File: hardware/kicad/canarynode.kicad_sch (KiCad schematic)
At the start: 26 parts, among them J1 Conn_01x02_Pin, SW1 SW_Push, U1 TPS62160DGK, U2 STM32G474RETx

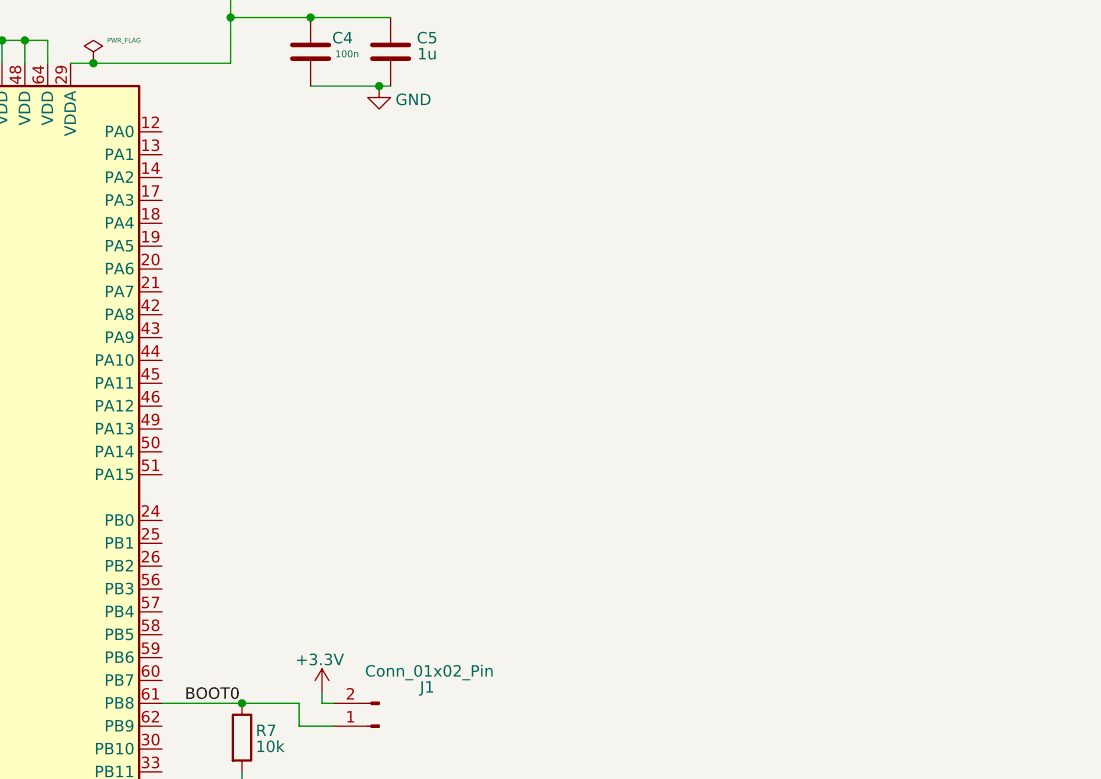
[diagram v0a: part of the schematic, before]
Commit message: schematic: add USB-C subcircuit (J2, U3, R8/R9, C14/C15)
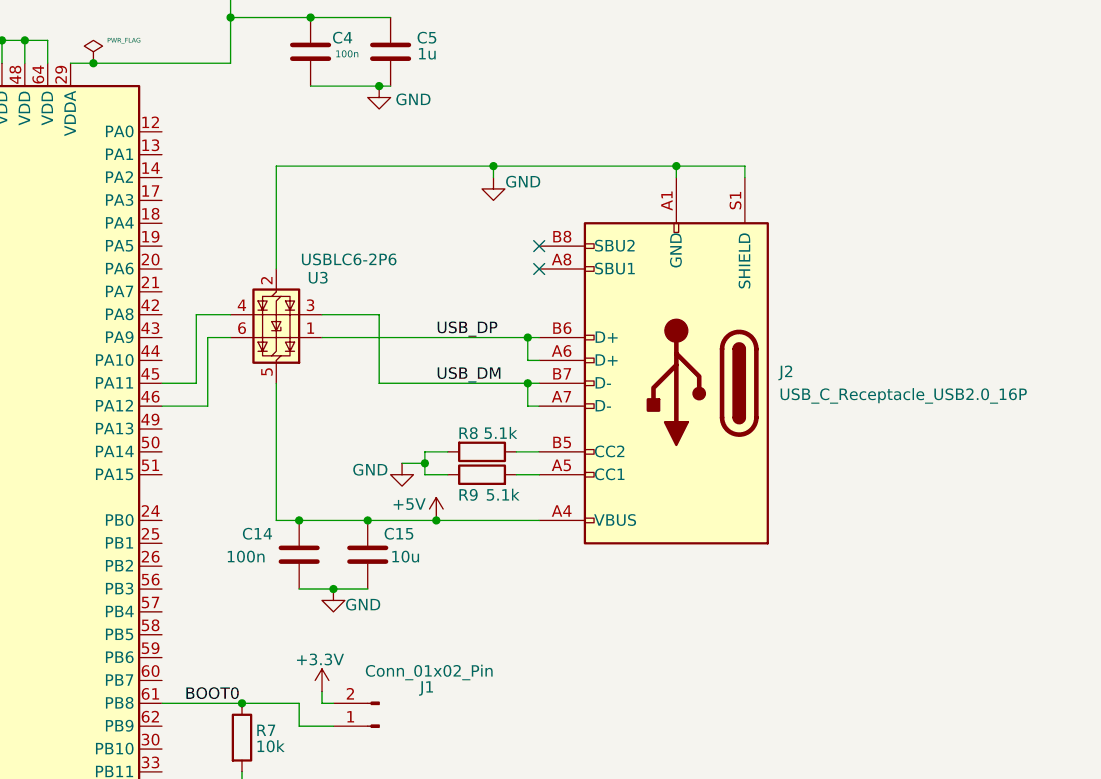
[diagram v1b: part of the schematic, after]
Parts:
- added C14: 100n, symbol Device:C
- added C15: 10u, symbol Device:C
- added J2: USB_C_Receptacle_USB2.0_16P, symbol Connector:USB_C_Receptacle_USB2.0_16P
- added R8, R9: 5.1k, symbol Device:R
- added U3: USBLC6-2P6, Package_TO_SOT_SMD:SOT-666, symbol Power_Protection:USBLC6-2P6
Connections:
- net +5V: now also C14.1, C15.1, J2.A4 (VBUS), J2.A9 (VBUS), J2.B4 (VBUS), J2.B9 (VBUS), U3.5 (VBUS)
- net GND: now also C14.2, C15.2, J2.A1 (GND), J2.A12 (GND), J2.B1 (GND), J2.B12 (GND), J2.S1 (SHIELD), R8.2, R9.1, U3.2 (GND)
- net at U2.45 (PA11): now also U3.4 (I/O2)
- net at U2.46 (PA12): now also U3.6 (I/O1)
- new net: J2.A5 (CC1), R9.2
- new net: J2.B5 (CC2), R8.1
- new net USB_DM: J2.A7 (D-), J2.B7 (D-), U3.3 (I/O2)
- new net USB_DP: J2.A6 (D+), J2.B6 (D+), U3.1 (I/O1)
- no-connect marks 0 -> 2

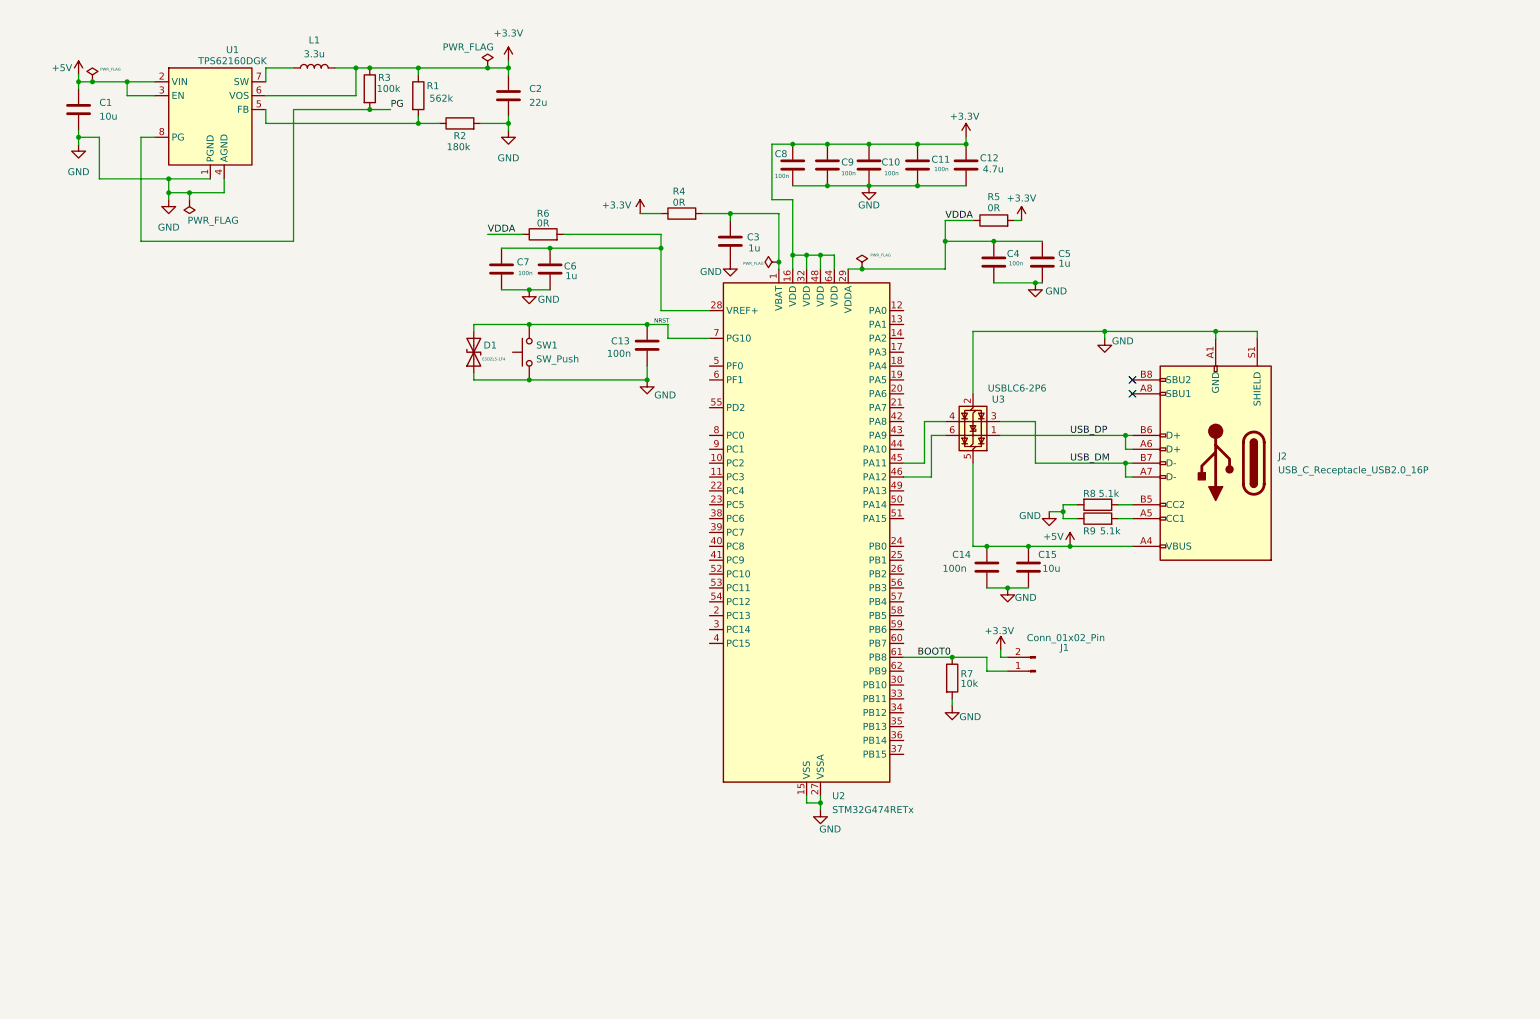
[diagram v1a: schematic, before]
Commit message: Add BME280 environmental sensor (U5, I2C1, addr 0x76)
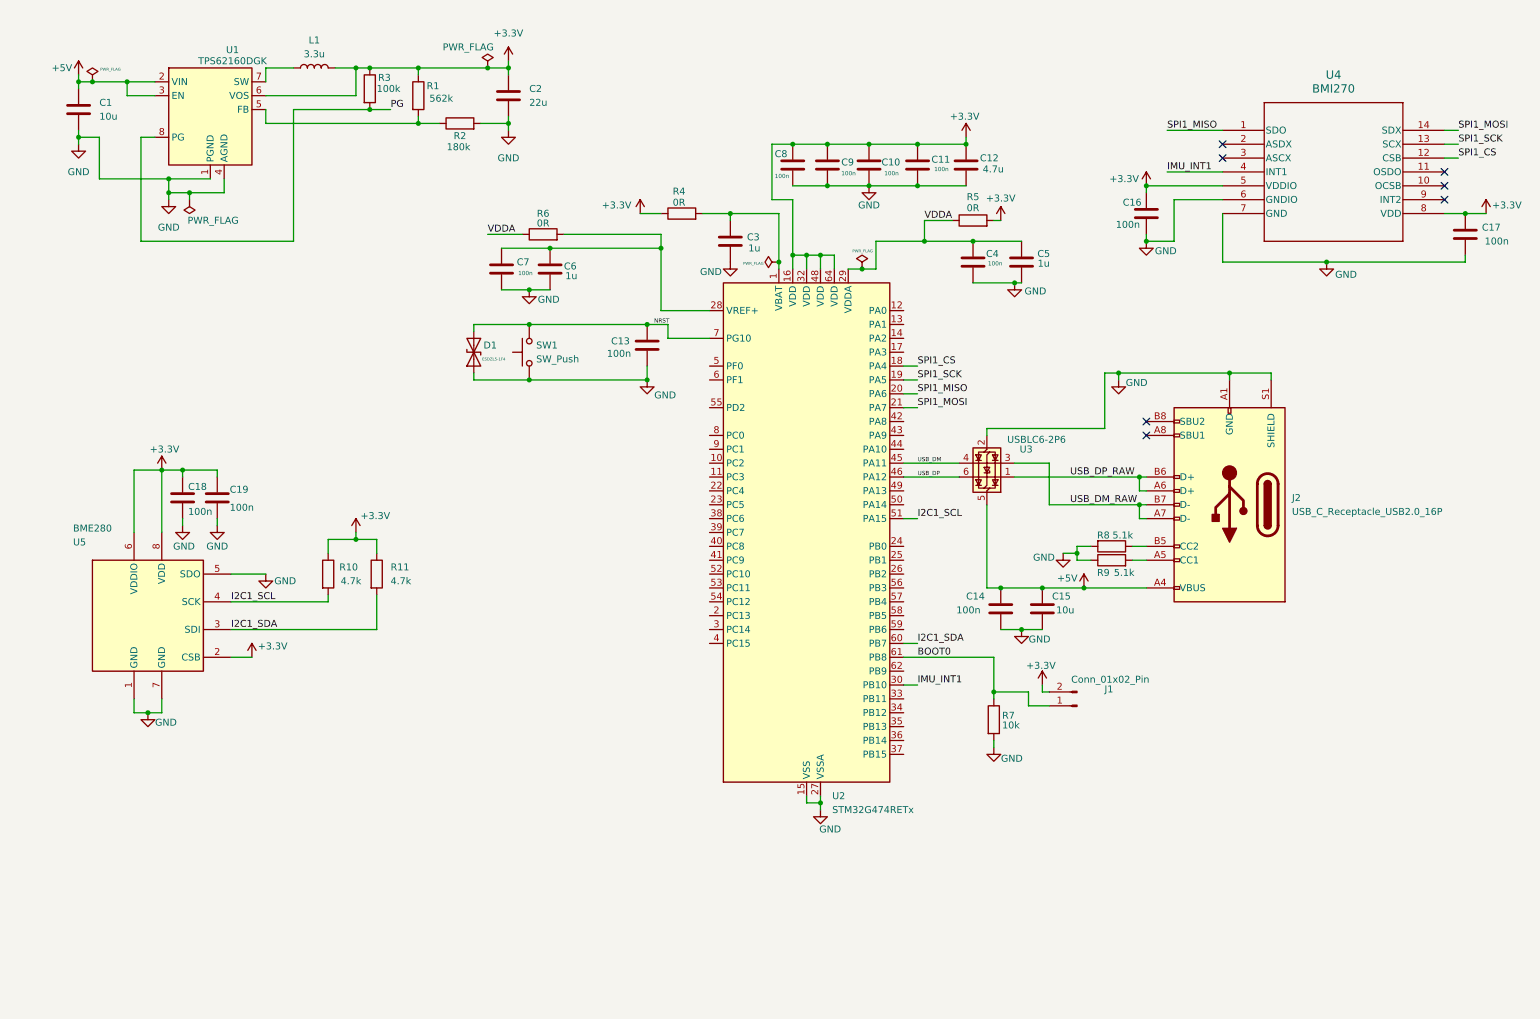
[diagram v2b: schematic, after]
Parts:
- added C16, C17, C18, C19: 100n, symbol Device:C
- added R10, R11: 4.7k, symbol Device:R
- added U4: BMI270, BMI270_BOS, symbol BMI270:BMI270
- added U5: BME280, Package_LGA:Bosch_LGA-8_2.5x2.5mm_P0.65mm_ClockwisePinNumbering, symbol Sensor:BME280
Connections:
- net +3.3V: now also C16.1, C17.1, C18.1, C19.1, R10.1, R11.1, U4.5 (VDDIO), U4.8 (VDD), U5.2 (CSB), U5.6 (VDDIO), U5.8 (VDD)
- net GND: now also C16.2, C17.2, C18.2, C19.2, U4.6 (GNDIO), U4.7 (GND), U5.1 (GND), U5.5 (SDO), U5.7 (GND)
- net USB_DM: now also U2.45 (PA11), U3.4 (I/O2); no longer J2.A7 (D-), J2.B7 (D-), U3.3 (I/O2)
- net USB_DP: now also U2.46 (PA12), U3.6 (I/O1); no longer J2.A6 (D+), J2.B6 (D+), U3.1 (I/O1)
- net SPI1_CS: now reaches U2.18 (PA4)
- net SPI1_CS: now also U4.12 (CSB)
- net SPI1_SCK: now reaches U2.19 (PA5)
- net SPI1_SCK: now also U4.13 (SCX)
- net SPI1_MISO: now reaches U2.20 (PA6)
- net SPI1_MISO: now also U4.1 (SDO)
- net SPI1_MOSI: now reaches U2.21 (PA7)
- net SPI1_MOSI: now also U4.14 (SDX)
- net IMU_INT1: now reaches U2.30 (PB10)
- net IMU_INT1: now also U4.4 (INT1)
- net I2C1_SCL: now reaches U2.51 (PA15)
- net I2C1_SCL: now also R10.2, U5.4 (SCK)
- net I2C1_SDA: now reaches U2.60 (PB7)
- net I2C1_SDA: now also R11.2, U5.3 (SDI)
- new net USB_DM_RAW: J2.A7 (D-), J2.B7 (D-), U3.3 (I/O2)
- new net USB_DP_RAW: J2.A6 (D+), J2.B6 (D+), U3.1 (I/O1)
- no-connect marks 2 -> 7
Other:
- moved on the sheet: C14, C15, C4, C5, J1, J2, R5, R7, R8, R9, U3

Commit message: Add CAN FD bus: TCAN334G transceiver, 120Ω switchable termination, PESD2CANFD27V TVS, 3.5mm screw terminal
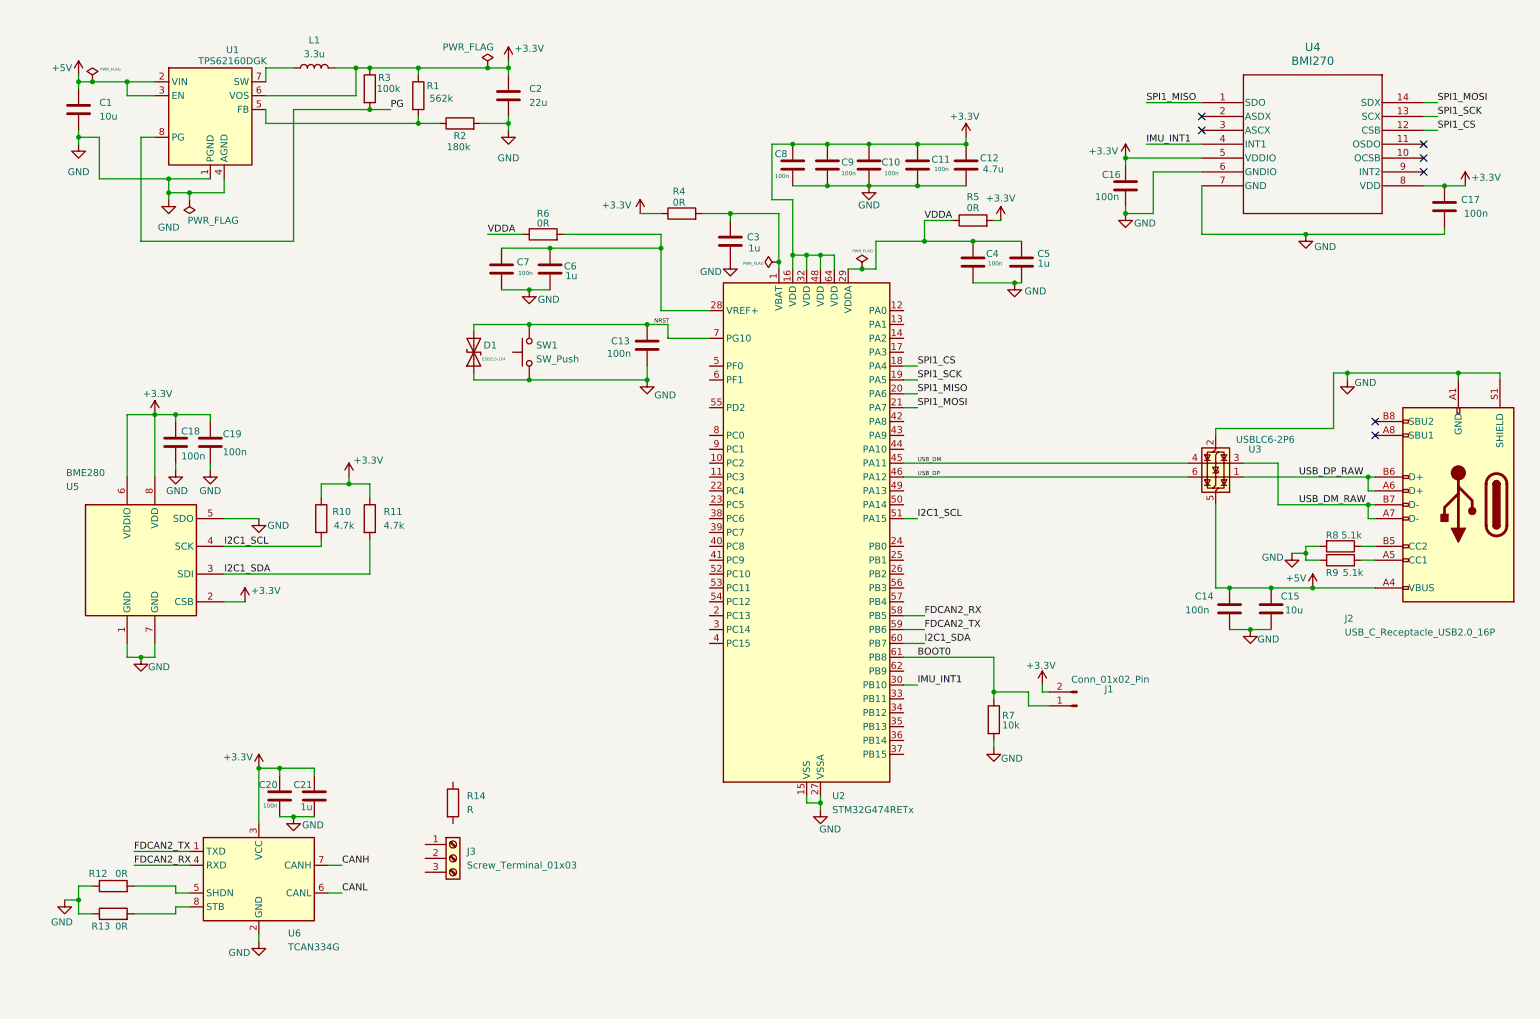
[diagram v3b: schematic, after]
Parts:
- added C20: 100n, symbol Device:C
- added C21: 1u, symbol Device:C
- added J3: Screw_Terminal_01x03, symbol Connector:Screw_Terminal_01x03
- added R12, R13: 0R, symbol Device:R
- added R14: R, symbol Device:R
- added U6: TCAN334G, symbol Interface_CAN_LIN:TCAN334G
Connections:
- net +3.3V: now also C20.1, C21.1, U6.3 (VCC)
- net GND: now also C20.2, C21.2, R12.1, R13.1, U6.2 (GND)
- net FDCAN2_RX: now reaches U2.58 (PB5)
- net FDCAN2_RX: now also U6.4 (RXD)
- net FDCAN2_TX: now reaches U2.59 (PB6)
- net FDCAN2_TX: now also U6.1 (TXD)
- new net: R13.2, U6.8 (STB)
- new net: R12.2, U6.5 (SHDN)
- new net CANH: U6.7 (CANH)
- new net CANL: U6.6 (CANL)
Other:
- moved on the sheet: C14, C15, C16, C17, C18, C19, J2, R10, R11, R8, R9, U3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

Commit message: Add LEDs, button, SWD header, UART header
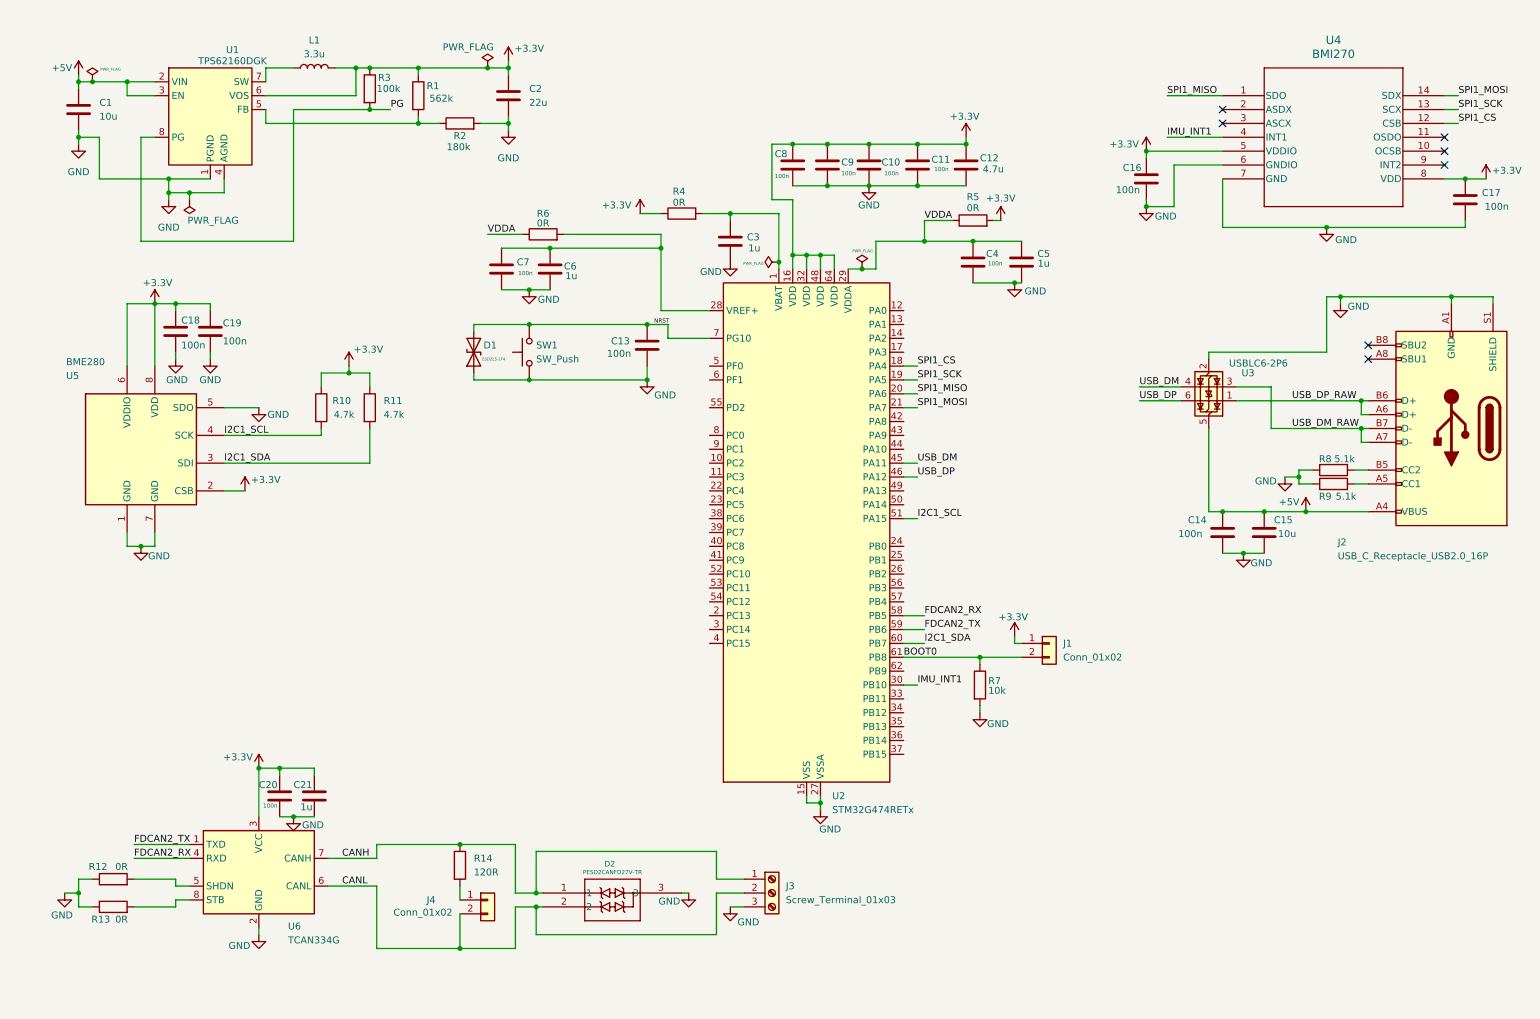
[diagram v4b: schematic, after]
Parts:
- removed J1: Conn_01x02_Pin, symbol Connector:Conn_01x02_Pin
- added D2: PESD2CANFD27V-TR, SOT23_PESD2_NEX, symbol PESD2CANFD24V:PESD2CANFD27V-TR
- added J1, J4: Conn_01x02, symbol Connector_Generic:Conn_01x02
- R14: value R -> 120R
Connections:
- net +3.3V: now also J1.1 (Pin_1)
- net BOOT0: now also J1.2 (Pin_2)
- net CANH: now also J3.1 (Pin_1), R14.1, D2.1
- net CANL: now also J3.2 (Pin_2), D2.2, J4.2 (Pin_2)
- net GND: now also J3.3 (Pin_3), D2.3
- net at R14.2: now also J4.1 (Pin_1)
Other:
- moved on the sheet: C14, C15, C16, C17, C18, C19, J2, J3, R10, R11, R12, R13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
